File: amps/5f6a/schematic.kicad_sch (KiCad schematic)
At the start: 64 parts, among them T3 2R sec

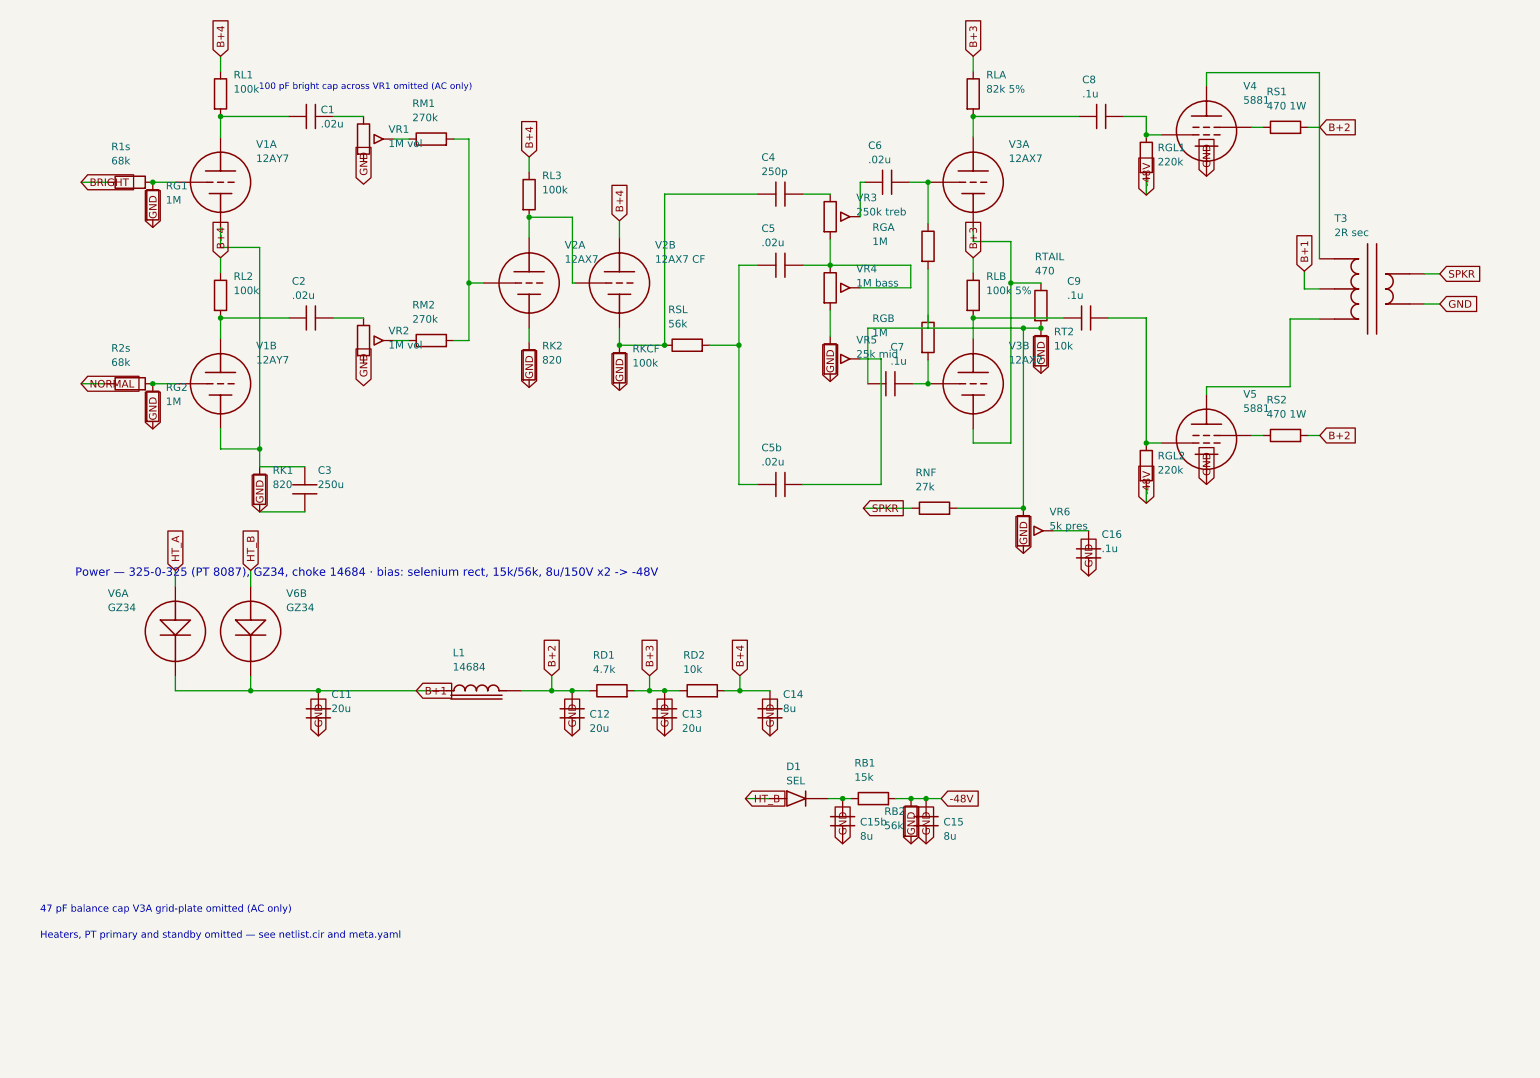
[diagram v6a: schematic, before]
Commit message: Fix: label-wire abutments the gate cannot see, caught by reading pixels
Four sites from the closing visual pass, each a designator or value line
sitting on live wiring below gate sensitivity (wires are not a clash class,
and the old placement ruler under-read text width):

- 5F6-A: RB2's block, squeezed into the 2.5 mm channel beside C15, printed
  through its own resistor body and into C15b's designator. Authored anchor
  now letters it above the supply wire, between RB1's lettering and the -48V
  flag — the one clear pocket in that cramped bias block.
- 6G4: the Speed pot's "4M-RA speed" value line lay on the oscillator ladder
  wire and CTO2's pin; anchored clear (the true-ruler placer settles it left
  of the pot).
- 6G5: RNFB's vertical lettering straddled the NFB wire itself. Drawn
  directly instead of via series_h so the block can be pinned horizontal
  under the part. Also: the tremolo caption was a 175 mm single-sentence
  banner — wider than any clear band on the sheet, printing across the bias
  diodes wherever it was placed. It keeps its headline beside the V3 bottle;
  the mechanism sentence is a note, and notes live in the band.
- 1959: both volume pots' "1M vol" crossed the wiper wire and RM1/RM2's
  pins; anchored clear of the pot body (placer settles them left).

6G6-B's RK2B/CK2B crowding (the fourth verdict item) needed no draw-script
change: the renderer-metric placer from the previous commit already moves the
block clear of the tie wire.

🤖 Generated with [Claude Code](https://claude.com/claude-code)

Co-Authored-By: Claude Fable 5 <noreply@anthropic.com>
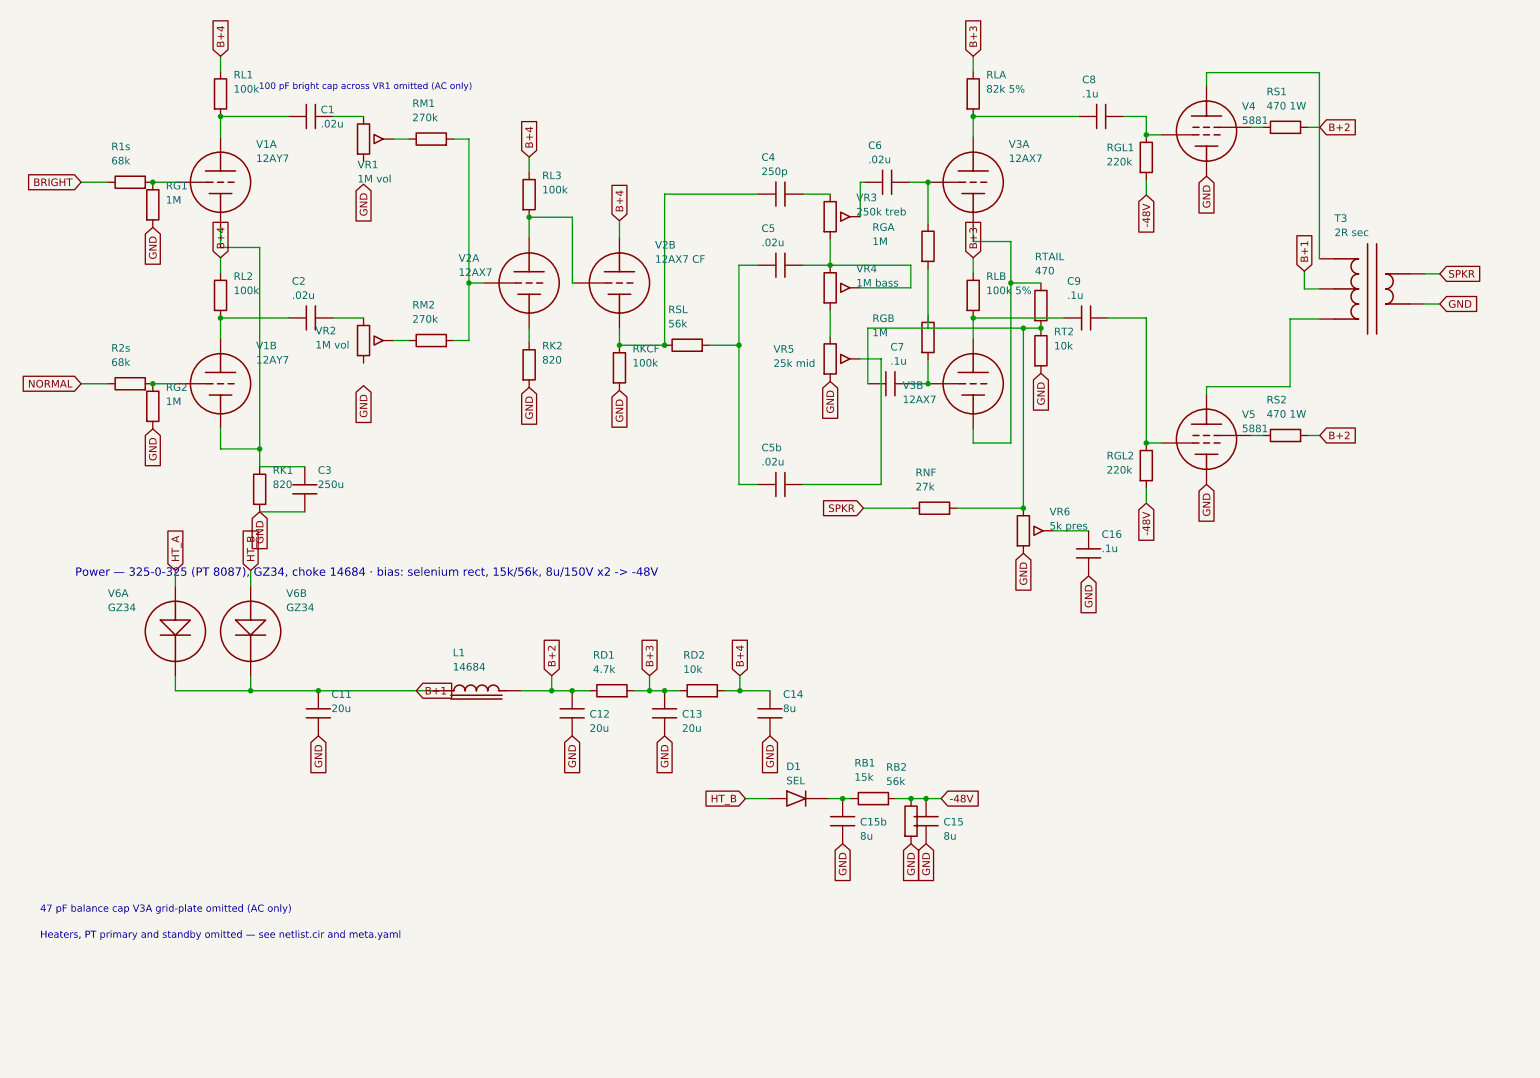
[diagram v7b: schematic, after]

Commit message: Fix: deterministic schematic ids and wires split at every join
- _u() is uuid5 over (amp id, emission order), so a regeneration of an
  unchanged script is byte-identical and a drift gate becomes possible
- write() splits wire segments at symbol pins, wire ends and junction dots,
  so the file connects exactly what the drawing shows under KiCad's
  endpoint-only semantics (270 pins were on a wire's interior; net
  partitions unchanged on all 38 sheets)
- all sheets regenerated; aa864-bassman title block was stale (draft) and
  now matches meta.yaml (verified)

Co-Authored-By: Claude Fable 5.1 <noreply@anthropic.com>
Claude-Session: https://claude.ai/code/session_01KBMfdh37HmCL2iWcBiL5J1
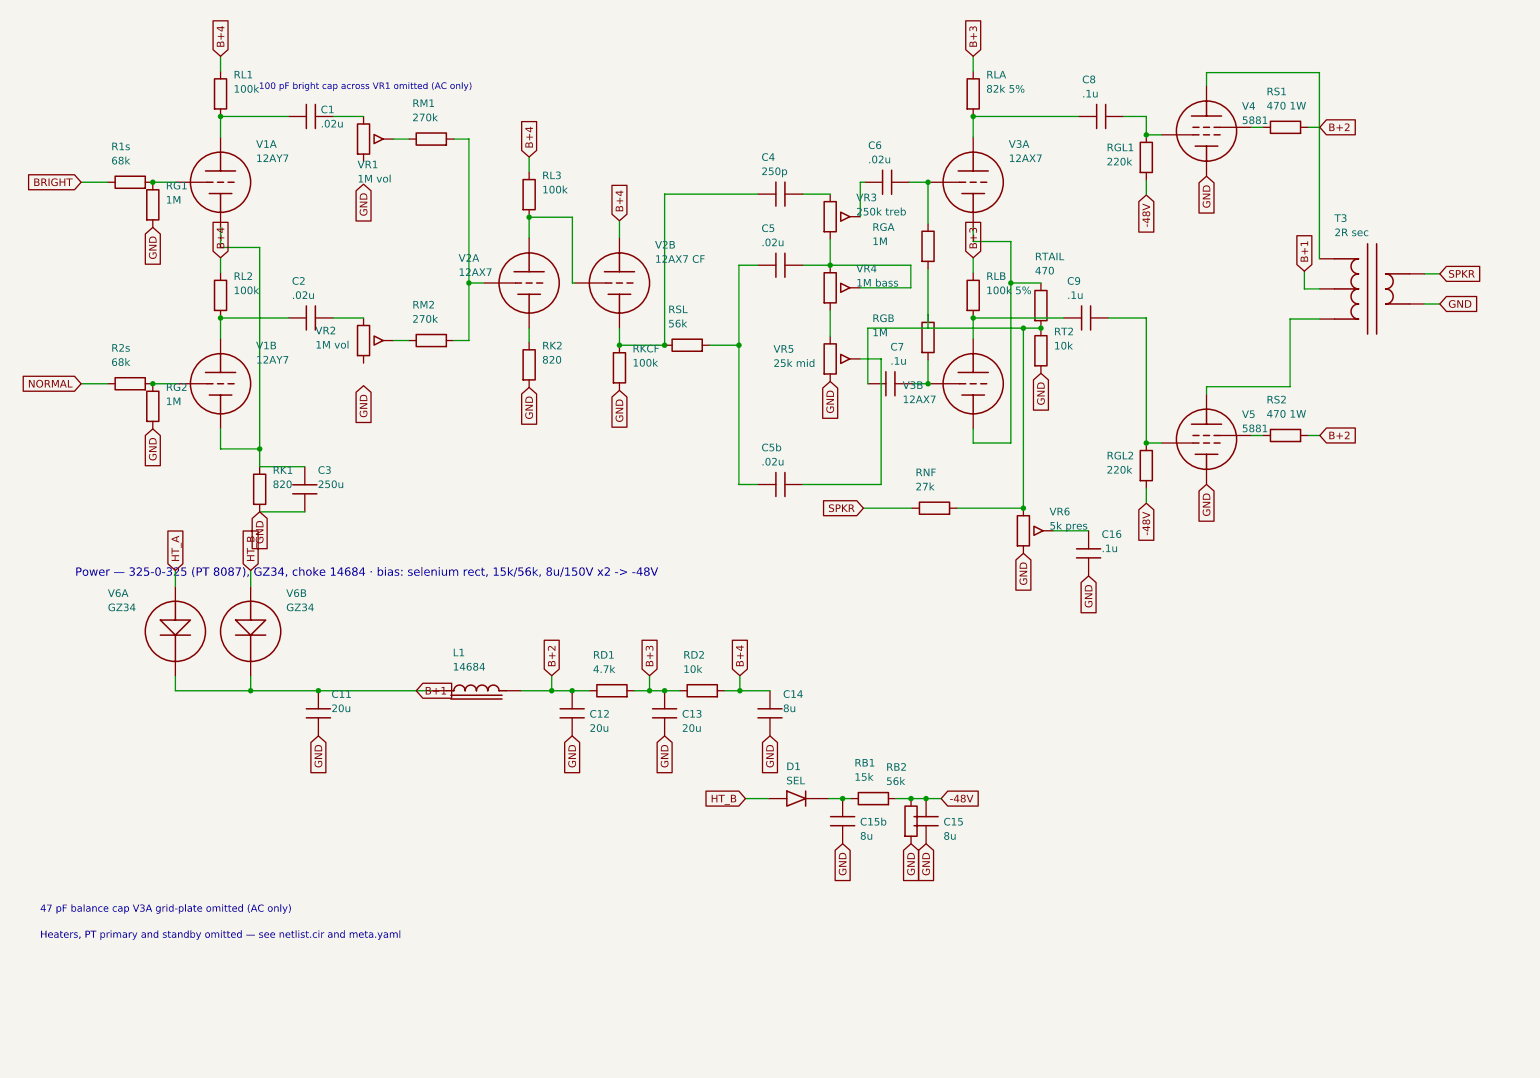
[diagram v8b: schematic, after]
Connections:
- net at RGB.1: now also C7.1, RGA.2, RNF.2, RT2.1, RTAIL.2, VR6.1
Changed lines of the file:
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@@
   (wire (pts (xy 43.1388 83.278) (xy 49.7388 83.278))
     (stroke (width 0) (type default)))
-  (wire (pts (xy 49.7388 49.278) (xy 49.7388 86.278))
+  (wire (pts (xy 49.7388 49.278) (xy 49.7388 83.278))
+    (stroke (width 0) (type default)))
+  (wire (pts (xy 49.7388 83.278) (xy 49.7388 86.278))
     (stroke (width 0) (type default)))
   (junction (at 49.7388 83.278) (diameter 0) (color 0 0 0 0))
@@
   (wire (pts (xy 170.139 82.278) (xy 176.489 82.278))
     (stroke (width 0) (type default)))
-  (wire (pts (xy 176.489 48.278) (xy 176.489 82.278))
+  (wire (pts (xy 176.489 48.278) (xy 176.489 55.278))
+    (stroke (width 0) (type default)))
+  (wire (pts (xy 176.489 55.278) (xy 176.489 82.278))
     (stroke (width 0) (type default)))
   (junction (at 176.489 55.278) (diameter 0) (color 0 0 0 0))
@@
     (property "Reference" "RGA" (at 153.119 45.888 0) (effects (font (size 1.27 1.27)) (justify left)))
     (property "Value" "1M" (at 153.119 48.288 0) (effects (font (size 1.27 1.27)) (justify left))))
-  (wire (pts (xy 162.519 52.898) (xy 162.519 62.898))
-    (stroke (width 0) (type default)))
-  (wire (pts (xy 162.519 62.898) (xy 181.569 62.898))
+  (wire (pts (xy 162.519 52.898) (xy 162.519 60.658))
+    (stroke (width 0) (type default)))
+  (wire (pts (xy 162.519 60.658) (xy 162.519 62.898))
+    (stroke (width 0) (type default)))
+  (wire (pts (xy 162.519 62.898) (xy 178.609 62.898))
+    (stroke (width 0) (type default)))
+  (wire (pts (xy 178.609 62.898) (xy 181.569 62.898))
     (stroke (width 0) (type default)))
   (wire (pts (xy 162.519 72.278) (xy 162.519 68.278))
@@
   (wire (pts (xy 48.2188 121.678) (xy 48.2188 124.078))
     (stroke (width 0) (type default)))
-  (wire (pts (xy 35.5188 124.078) (xy 76.1588 124.078))
+  (wire (pts (xy 35.5188 124.078) (xy 48.2188 124.078))
+    (stroke (width 0) (type default)))
+  (wire (pts (xy 48.2188 124.078) (xy 59.6488 124.078))
+    (stroke (width 0) (type default)))
+  (wire (pts (xy 59.6488 124.078) (xy 76.1588 124.078))
     (stroke (width 0) (type default)))
   (junction (at 48.2188 124.078) (diameter 0) (color 0 0 0 0))
@@
     (property "Reference" "L1" (at 82.3188 117.678 0) (effects (font (size 1.27 1.27)) (justify left)))
     (property "Value" "14684" (at 82.3188 120.078 0) (effects (font (size 1.27 1.27)) (justify left))))
-  (wire (pts (xy 93.9388 124.078) (xy 105.369 124.078))
+  (wire (pts (xy 93.9388 124.078) (xy 99.0188 124.078))
+    (stroke (width 0) (type default)))
+  (wire (pts (xy 99.0188 124.078) (xy 102.469 124.078))
+    (stroke (width 0) (type default)))
+  (wire (pts (xy 102.469 124.078) (xy 105.369 124.078))
     (stroke (width 0) (type default)))
   (junction (at 99.0188 124.078) (diameter 0) (color 0 0 0 0))
@@
     (property "Reference" "RD1" (at 105.979 118.078 270) (effects (font (size 1.27 1.27)) (justify left)))
     (property "Value" "4.7k" (at 105.979 120.478 270) (effects (font (size 1.27 1.27)) (justify left))))
-  (wire (pts (xy 112.989 124.078) (xy 120.609 124.078))
+  (wire (pts (xy 112.989 124.078) (xy 115.529 124.078))
+    (stroke (width 0) (type default)))
+  (wire (pts (xy 115.529 124.078) (xy 118.069 124.078))
+    (stroke (width 0) (type default)))
+  (wire (pts (xy 118.069 124.078) (xy 120.609 124.078))
     (stroke (width 0) (type default)))
   (junction (at 115.529 124.078) (diameter 0) (color 0 0 0 0))
@@
     (property "Reference" "RD2" (at 121.219 118.078 270) (effects (font (size 1.27 1.27)) (justify left)))
     (property "Value" "10k" (at 121.219 120.478 270) (effects (font (size 1.27 1.27)) (justify left))))
-  (wire (pts (xy 128.229 124.078) (xy 135.849 124.078))
+  (wire (pts (xy 128.229 124.078) (xy 130.769 124.078))
+    (stroke (width 0) (type default)))
+  (wire (pts (xy 130.769 124.078) (xy 135.849 124.078))
     (stroke (width 0) (type default)))
   (junction (at 130.769 124.078) (diameter 0) (color 0 0 0 0))
@@
     (property "Reference" "D1" (at 138.599 136.878 0) (effects (font (size 1.27 1.27)) (justify left)))
     (property "Value" "SEL" (at 138.599 139.278 0) (effects (font (size 1.27 1.27)) (justify left))))
-  (wire (pts (xy 145.679 142.278) (xy 149.489 142.278))
+  (wire (pts (xy 145.679 142.278) (xy 148.109 142.278))
+    (stroke (width 0) (type default)))
+  (wire (pts (xy 148.109 142.278) (xy 149.489 142.278))
     (stroke (width 0) (type default)))
   (junction (at 148.109 142.278) (diameter 0) (color 0 0 0 0))
@@
   (wire (pts (xy 149.489 142.278) (xy 149.489 142.278))
     (stroke (width 0) (type default)))
-  (wire (pts (xy 157.109 142.278) (xy 164.729 142.278))
+  (wire (pts (xy 157.109 142.278) (xy 159.649 142.278))
+    (stroke (width 0) (type default)))
+  (wire (pts (xy 159.649 142.278) (xy 162.189 142.278))
+    (stroke (width 0) (type default)))
+  (wire (pts (xy 162.189 142.278) (xy 164.729 142.278))
     (stroke (width 0) (type default)))
   (junction (at 159.649 142.278) (diameter 0) (color 0 0 0 0))
